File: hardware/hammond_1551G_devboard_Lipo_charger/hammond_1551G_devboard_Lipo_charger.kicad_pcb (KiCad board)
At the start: 4 copper layers, 44 x 29 mm, 6 parts, among them J1 DevBoardDigital, J2 DevBoardAnalog

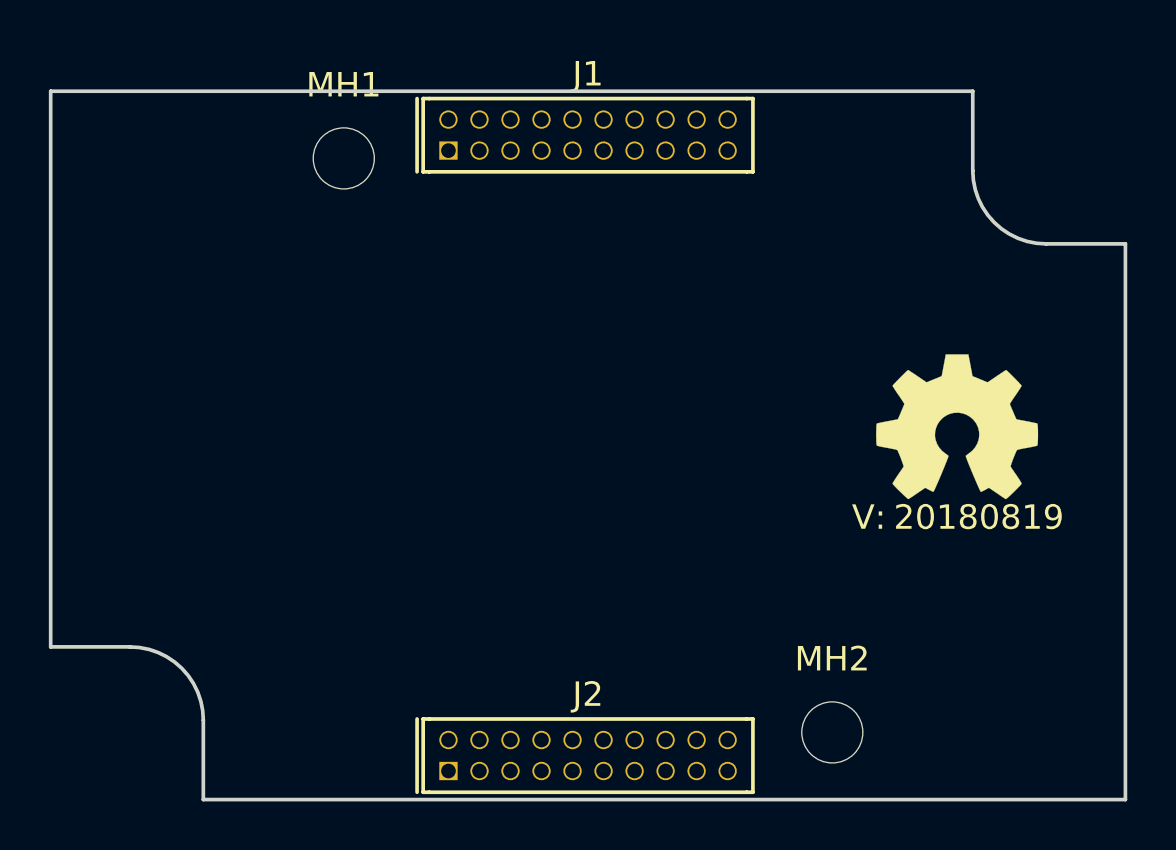
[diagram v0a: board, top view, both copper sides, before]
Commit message: power regulator started and started little bit of layout
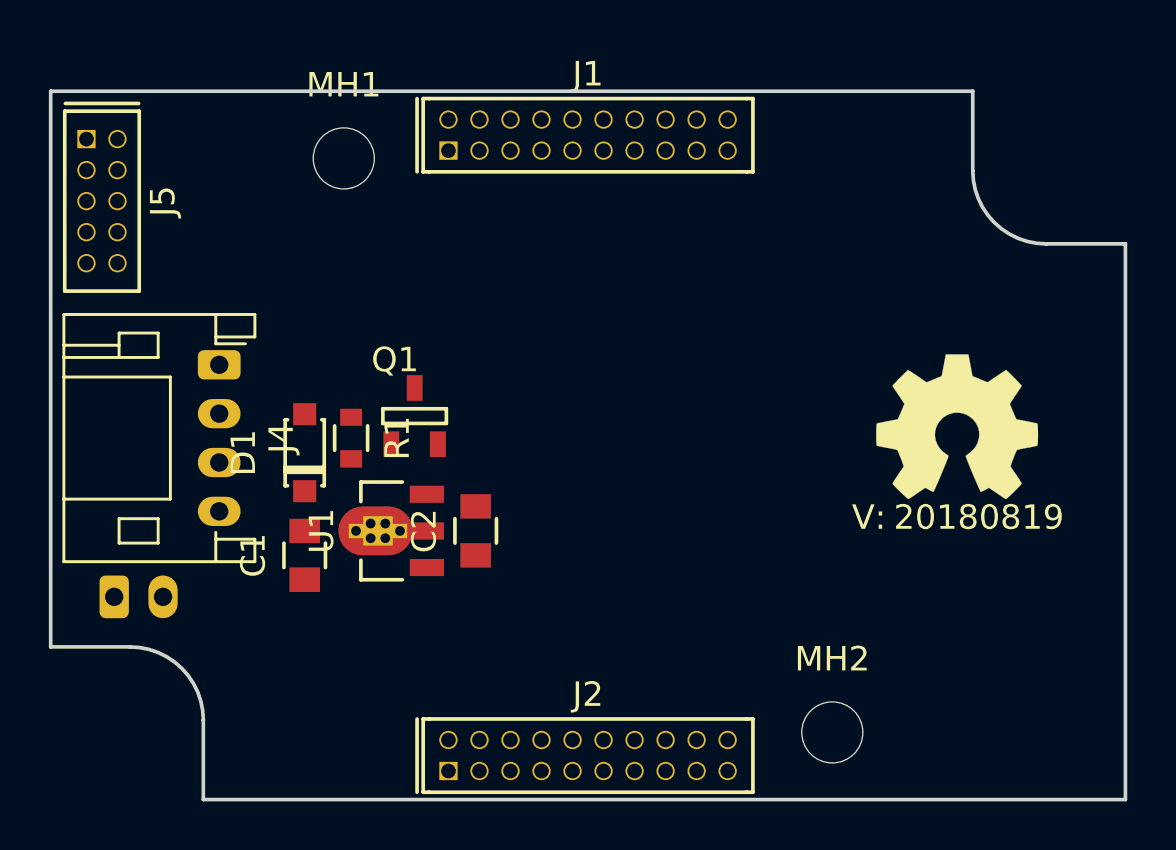
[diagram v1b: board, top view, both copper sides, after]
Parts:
- added C1: 1u, SquantorRcl:C_0805, F.Cu at (48.7, 167.3)
- added C2: 10u, SquantorRcl:C_0805, F.Cu at (55.7, 166.3)
- added D1: NSR0320, SquantorDiodes:SOD-123, F.Cu at (48.7, 163.1)
- added J3: Battery_2pin, Connector_JST:JST_PH_S2B-PH-K_1x02_P2.00mm_Horizontal, B.Cu at (40.9, 169.0)
- added J4: DevBoardUartInput, Connector_JST:JST_PH_S4B-PH-K_1x04_P2.00mm_Horizontal, F.Cu at (45.2, 159.5)
- added J5: JTAG_2X05, SquantorConnectors:Header-0127-2X05-H006, F.Cu at (40.4, 152.8)
- added Q1: Q_NMOS_GSD, SquantorIC:SOT23-3-Microchip-TT, F.Cu at (53.2, 161.6)
- added R1: R, SquantorRcl:R_0603_hand, F.Cu at (50.6, 162.5)
- added U1: MCP1702-MB, SquantorIC:SOT89-ViaTab-Microchip-MB, F.Cu at (53.7, 166.3)
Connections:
- net VCC renamed VBUS
- J1 pad 10: (no net) -> Net-(J1-Pad10)
- J1 pad 11: (no net) -> Net-(J1-Pad11)
- J1 pad 12: (no net) -> Net-(J1-Pad12)
- J1 pad 13: (no net) -> Net-(J1-Pad13)
- J1 pad 14: (no net) -> Net-(J1-Pad14)
- J1 pad 15: (no net) -> Net-(J1-Pad15)
- J1 pad 16: (no net) -> Net-(J1-Pad16)
- J1 pad 17: (no net) -> Net-(J1-Pad17)
- J1 pad 18: (no net) -> Net-(J1-Pad18)
- J1 pad 19: (no net) -> Net-(J1-Pad19)
- J1 pad 20: (no net) -> Net-(J1-Pad20)
- J1 pad 5: (no net) -> Net-(J1-Pad5)
- J1 pad 6: (no net) -> Net-(J1-Pad6)
- J1 pad 7: (no net) -> Net-(J1-Pad7)
- J1 pad 8: (no net) -> Net-(J1-Pad8)
- J1 pad 9: (no net) -> Net-(J1-Pad9)
- J2 pad 10: (no net) -> Net-(J2-Pad10)
- J2 pad 11: (no net) -> Net-(J2-Pad11)
- J2 pad 12: (no net) -> Net-(J2-Pad12)
- J2 pad 13: (no net) -> Net-(J2-Pad13)
- J2 pad 14: (no net) -> Net-(J2-Pad14)
- J2 pad 15: (no net) -> Net-(J2-Pad15)
- J2 pad 16: (no net) -> Net-(J2-Pad16)
- J2 pad 17: (no net) -> Net-(J2-Pad17)
- J2 pad 18: (no net) -> Net-(J2-Pad18)
- J2 pad 19: (no net) -> Net-(J2-Pad19)
- J2 pad 20: (no net) -> Net-(J2-Pad20)
- J2 pad 3: VSS -> +BATT
- J2 pad 4: VSS -> +BATT
- J2 pad 9: (no net) -> Net-(J2-Pad9)

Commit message: further schematic layout with power joining and some experiments
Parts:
- added U2: power_joiner_2_nets, SquantorSpecial:power_joiner_2_conn_06mm, F.Cu at (57.5, 166.8)
- added U3: power_joiner_2_nets, SquantorSpecial:power_joiner_2_conn_06mm, F.Cu at (57.5, 167.7)
- added U4: power_joiner_2_nets, SquantorSpecial:power_joiner_2_conn_06mm, F.Cu at (57.5, 165.5)
- added U5: power_joiner_2_nets, SquantorSpecial:power_joiner_2_conn_06mm, F.Cu at (57.5, 164.6)
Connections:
- J1 pad 10: Net-(J1-Pad10) -> (no net)
- J1 pad 11: Net-(J1-Pad11) -> (no net)
- J1 pad 12: Net-(J1-Pad12) -> (no net)
- J1 pad 13: Net-(J1-Pad13) -> (no net)
- J1 pad 14: Net-(J1-Pad14) -> (no net)
- J1 pad 15: Net-(J1-Pad15) -> (no net)
- J1 pad 16: Net-(J1-Pad16) -> (no net)
- J1 pad 17: Net-(J1-Pad17) -> (no net)
- J1 pad 18: Net-(J1-Pad18) -> (no net)
- J1 pad 19: Net-(J1-Pad19) -> (no net)
- J1 pad 20: Net-(J1-Pad20) -> (no net)
- J1 pad 5: Net-(J1-Pad5) -> (no net)
- J1 pad 6: Net-(J1-Pad6) -> (no net)
- J1 pad 7: Net-(J1-Pad7) -> (no net)
- J1 pad 8: Net-(J1-Pad8) -> (no net)
- J1 pad 9: Net-(J1-Pad9) -> (no net)
- J2 pad 10: Net-(J2-Pad10) -> (no net)
- J2 pad 11: Net-(J2-Pad11) -> (no net)
- J2 pad 12: Net-(J2-Pad12) -> (no net)
- J2 pad 13: Net-(J2-Pad13) -> (no net)
- J2 pad 14: Net-(J2-Pad14) -> (no net)
- J2 pad 15: Net-(J2-Pad15) -> (no net)
- J2 pad 16: Net-(J2-Pad16) -> (no net)
- J2 pad 17: Net-(J2-Pad17) -> (no net)
- J2 pad 18: Net-(J2-Pad18) -> (no net)
- J2 pad 19: Net-(J2-Pad19) -> (no net)
- J2 pad 20: Net-(J2-Pad20) -> (no net)
- J2 pad 9: Net-(J2-Pad9) -> (no net)
- J4 pad 3: /UART_TX -> Net-(J4-Pad3)
- J4 pad 4: /UART_RX -> Net-(J4-Pad3)
- J5 pad 10: Net-(J5-Pad10) -> (no net)
- J5 pad 2: Net-(J5-Pad2) -> (no net)
- J5 pad 4: Net-(J5-Pad4) -> (no net)
- J5 pad 6: Net-(J5-Pad6) -> (no net)
- J5 pad 7: Net-(J5-Pad7) -> (no net)
- J5 pad 8: Net-(J5-Pad8) -> (no net)

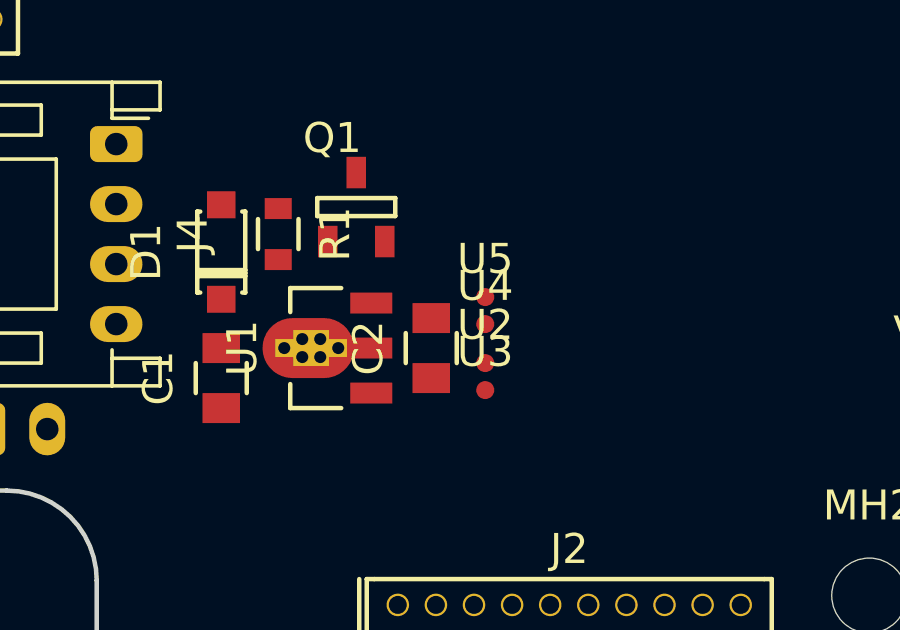
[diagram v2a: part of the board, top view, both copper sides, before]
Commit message: tried out if component copper graphics will get cleared by the plane fill algorithm
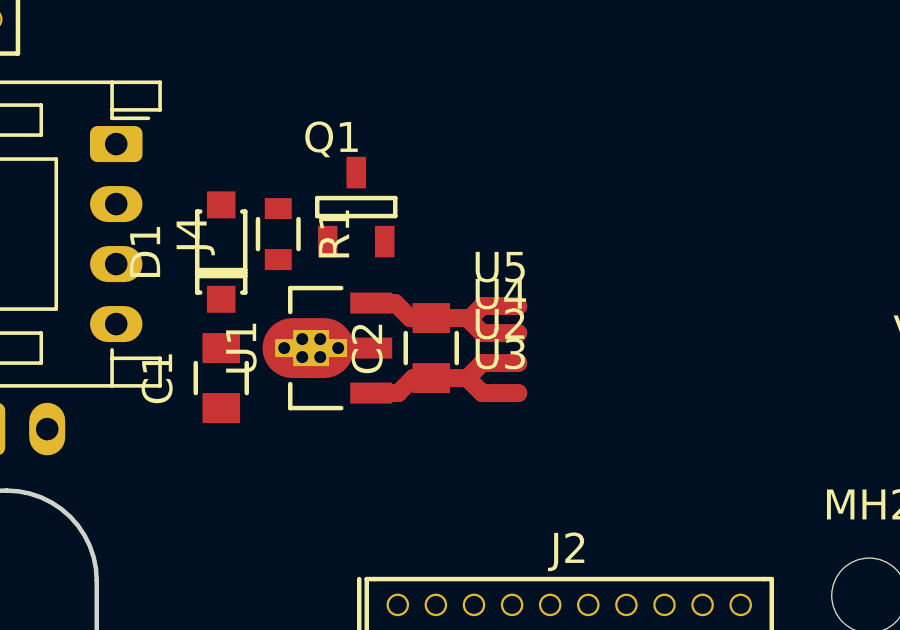
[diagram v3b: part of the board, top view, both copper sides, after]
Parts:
- moved U4 0.58 mm to (58.0, 165.8)
- moved U5 0.58 mm to (58.0, 164.9)
- moved U3 0.51 mm to (58.0, 167.8)
- moved U2 0.50 mm to (58.0, 166.8)
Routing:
- net GND: track 0.00 -> 4.82 mm
- net Net-(C2-Pad2): track 0.00 -> 4.74 mm
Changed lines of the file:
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@@
     (thickness 1.6)
     (drawings 10)
-    (tracks 0)
+    (tracks 13)
     (zones 0)
     (modules 19)
@@
   )
   (setup
-    (last_trace_width 0.127)
+    (last_trace_width 0.6)
     (user_trace_width 0.127)
     (user_trace_width 0.2)
@@
     (user_trace_width 2)
     (trace_clearance 0.127)
-    (zone_clearance 0.508)
+    (zone_clearance 0.2)
     (zone_45_only no)
     (trace_min 0.127)
@@
   )
   (module SquantorSpecial:power_joiner_2_conn_06mm (layer F.Cu)
-    (at 57.5 166.8)
+    (at 58 166.8)
     (fp_text reference U2 (at 0 -1.27) (layer F.SilkS)
       (effects (font (size 1 1) (thickness 0.15)))
@@
       (effects (font (size 1 1) (thickness 0.15)))
     )
-    (pad 2 smd circle (at 0 0) (size 0.6 0.6) (layers F.Cu F.Mask)
+    (fp_line (start 0.6 0) (end -0.6 0) (layer F.Cu) (width 0.6))
+    (pad 1 smd circle (at -0.6 0) (size 0.6 0.6) (layers F.Cu)
+      (net 5 GND))
+    (pad 2 smd circle (at 0.6 0) (size 0.6 0.6) (layers F.Cu)
       (net 2 VSS))
-    (pad 1 smd circle (at 0 0) (size 0.6 0.6) (layers F.Cu F.Mask)
-      (net 5 GND))
   )
   (module SquantorSpecial:power_joiner_2_conn_06mm (layer F.Cu)
-    (at 57.5 167.7)
+    (at 58 167.8)
     (fp_text reference U3 (at 0 -1.27) (layer F.SilkS)
       (effects (font (size 1 1) (thickness 0.15)))
@@
       (effects (font (size 1 1) (thickness 0.15)))
     )
-    (pad 1 smd circle (at 0 0) (size 0.6 0.6) (layers F.Cu F.Mask)
-      (net 5 GND))
-    (pad 2 smd circle (at 0 0) (size 0.6 0.6) (layers F.Cu F.Mask)
+    (fp_line (start 0.6 0) (end -0.6 0) (layer F.Cu) (width 0.6))
+    (pad 2 smd circle (at 0.6 0) (size 0.6 0.6) (layers F.Cu)
       (net 4 VSSA))
+    (pad 1 smd circle (at -0.6 0) (size 0.6 0.6) (layers F.Cu)
+      (net 5 GND))
   )
   (module SquantorSpecial:power_joiner_2_conn_06mm (layer F.Cu)
-    (at 57.5 165.5)
+    (at 58 165.8)
     (fp_text reference U4 (at 0 -1.27) (layer F.SilkS)
       (effects (font (size 1 1) (thickness 0.15)))
@@
       (effects (font (size 1 1) (thickness 0.15)))
     )
-    (pad 1 smd circle (at 0 0) (size 0.6 0.6) (layers F.Cu F.Mask)
+    (fp_line (start 0.6 0) (end -0.6 0) (layer F.Cu) (width 0.6))
+    (pad 2 smd circle (at 0.6 0) (size 0.6 0.6) (layers F.Cu)
+      (net 3 VDDA))
+    (pad 1 smd circle (at -0.6 0) (size 0.6 0.6) (layers F.Cu)
       (net 7 "Net-(C2-Pad2)"))
-    (pad 2 smd circle (at 0 0) (size 0.6 0.6) (layers F.Cu F.Mask)
-      (net 3 VDDA))
   )
   (module SquantorSpecial:power_joiner_2_conn_06mm (layer F.Cu)
-    (at 57.5 164.6)
+    (at 58 164.9)
     (fp_text reference U5 (at 0 -1.27) (layer F.SilkS)
       (effects (font (size 1 1) (thickness 0.15)))
@@
       (effects (font (size 1 1) (thickness 0.15)))
     )
-    (pad 2 smd circle (at 0 0) (size 0.6 0.6) (layers F.Cu F.Mask)
+    (fp_line (start 0.6 0) (end -0.6 0) (layer F.Cu) (width 0.6))
+    (pad 1 smd circle (at -0.6 0) (size 0.6 0.6) (layers F.Cu)
+      (net 7 "Net-(C2-Pad2)"))
+    (pad 2 smd circle (at 0.6 0) (size 0.6 0.6) (layers F.Cu)
       (net 1 VDD))
-    (pad 1 smd circle (at 0 0) (size 0.6 0.6) (layers F.Cu F.Mask)
-      (net 7 "Net-(C2-Pad2)"))
   )
   (gr_arc (start 41.55 174.05) (end 44.55 174.05) (angle -90) (layer Edge.Cuts) (width 0.15))
@@
   (gr_line (start 76.05 148.3) (end 76.05 151.55) (layer Edge.Cuts) (width 0.15))
   (gr_line (start 38.3 148.3) (end 76.05 148.3) (layer Edge.Cuts) (width 0.15))
+  (segment (start 56.9 167.3) (end 57.4 166.8) (width 0.6) (layer F.Cu) (net 5))
+  (segment (start 55.7 167.3) (end 56.9 167.3) (width 0.6) (layer F.Cu) (net 5))
+  (segment (start 56.9 167.3) (end 57.4 167.8) (width 0.6) (layer F.Cu) (net 5))
+  (segment (start 53.7 167.8) (end 54.6 167.8) (width 0.6) (layer F.Cu) (net 5))
+  (segment (start 55.1 167.3) (end 55.7 167.3) (width 0.6) (layer F.Cu) (net 5))
+  (segment (start 54.6 167.8) (end 55.1 167.3) (width 0.6) (layer F.Cu) (net 5))
+  (segment (start 57 165.3) (end 57.4 164.9) (width 0.6) (layer F.Cu) (net 7))
+  (segment (start 55.7 165.3) (end 57 165.3) (width 0.6) (layer F.Cu) (net 7))
+  (segment (start 57 165.4) (end 57.4 165.8) (width 0.6) (layer F.Cu) (net 7))
+  (segment (start 57 165.3) (end 57 165.4) (width 0.6) (layer F.Cu) (net 7))
+  (segment (start 53.7 164.8) (end 54.5 164.8) (width 0.6) (layer F.Cu) (net 7))
+  (segment (start 55 165.3) (end 55.7 165.3) (width 0.6) (layer F.Cu) (net 7))
+  (segment (start 54.5 164.8) (end 55 165.3) (width 0.6) (layer F.Cu) (net 7))
 )

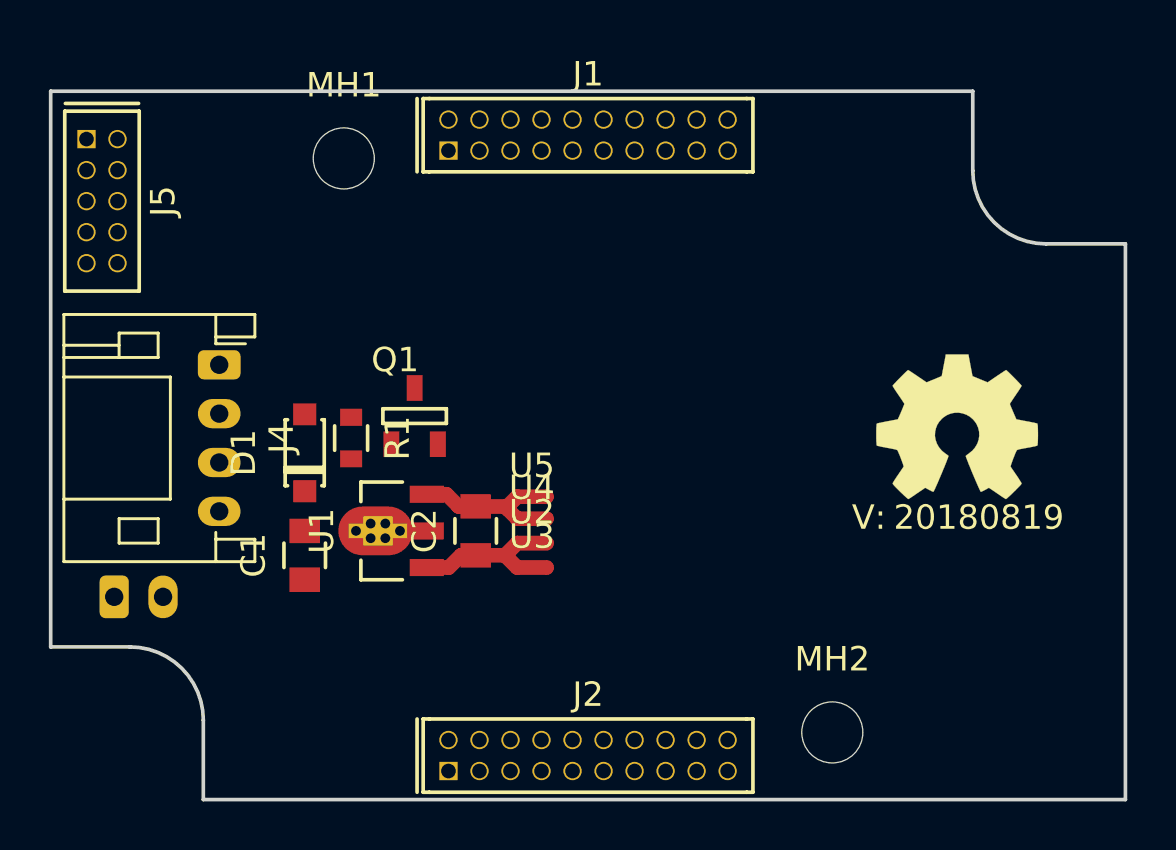
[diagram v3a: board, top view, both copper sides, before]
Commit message: added lipo charging schematic, starting initial layout on pcb
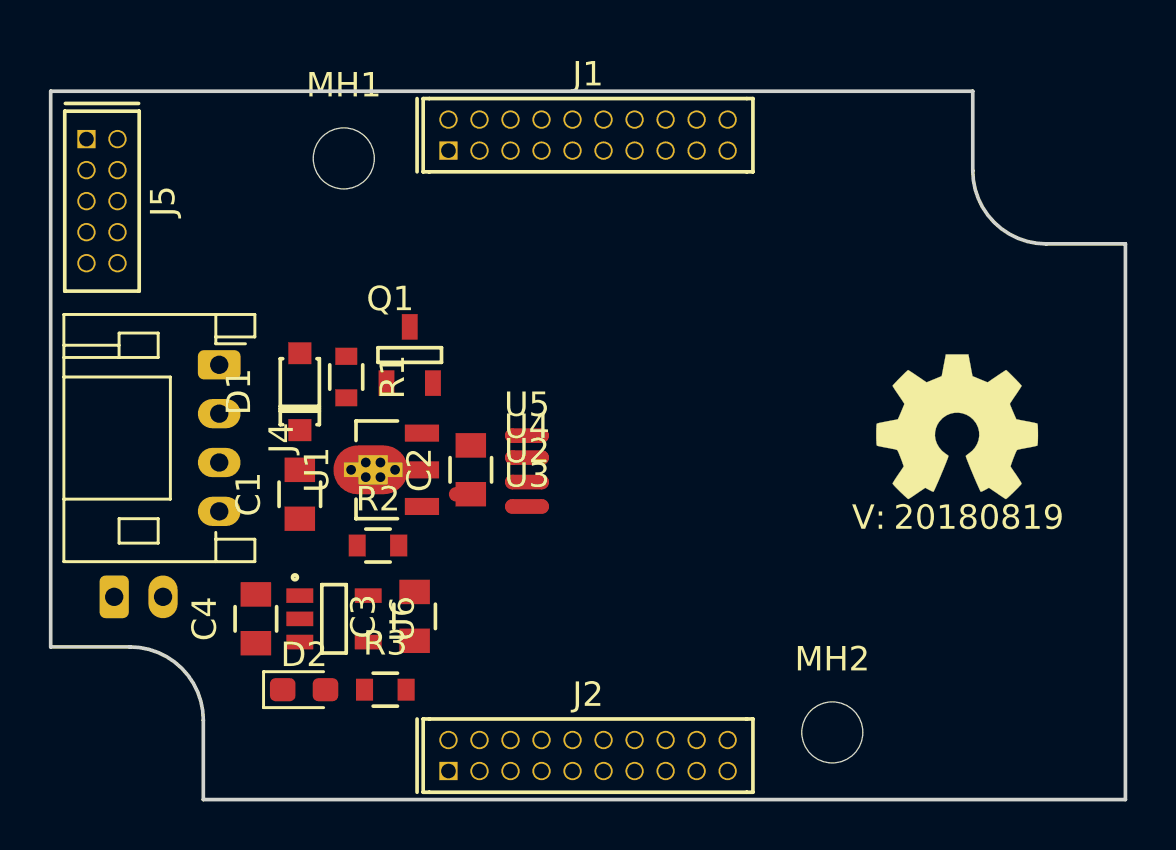
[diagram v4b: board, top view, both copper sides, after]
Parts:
- added C3: 10u, SquantorRcl:C_0805, F.Cu at (53.2, 169.8)
- added C4: 10u, SquantorRcl:C_0805, F.Cu at (46.7, 169.9)
- added D2: LED, LED_SMD:LED_0603_1608Metric_Pad1.05x0.95mm_HandSolder, F.Cu at (48.7, 172.8)
- added R2: 22K, SquantorRcl:R_0603_hand, F.Cu at (51.7, 166.9)
- added R3: 1k, SquantorRcl:R_0603_hand, F.Cu at (52.0, 172.8)
- added U6: MCP738312-OT, SquantorIC:SOT23-5-Microchip-OT, F.Cu at (49.9, 169.9)
- moved C1 2.51 mm to (48.5, 164.8)
- moved C2 2.51 mm to (55.5, 163.8)
- moved D1 2.51 mm to (48.5, 160.6)
- moved Q1 2.51 mm to (53.0, 159.1)
- moved R1 2.51 mm to (50.4, 160.0)
- moved U1 2.51 mm to (53.5, 163.8)
- moved U2 2.51 mm to (57.8, 164.3)
- moved U3 2.51 mm to (57.8, 165.3)
- moved U4 2.51 mm to (57.8, 163.3)
- moved U5 2.51 mm to (57.8, 162.4)
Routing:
- net Net-(C2-Pad2): track 4.74 -> 0.00 mm
- net GND: track 4.82 -> 0.60 mm
